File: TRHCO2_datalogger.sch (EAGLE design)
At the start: 31 parts, among them J3 USB-MICROB, U1 ATMEGA328P-MU, U7 SHT31/35, U8 MCP1703/3.3V, Y1 16MHZ

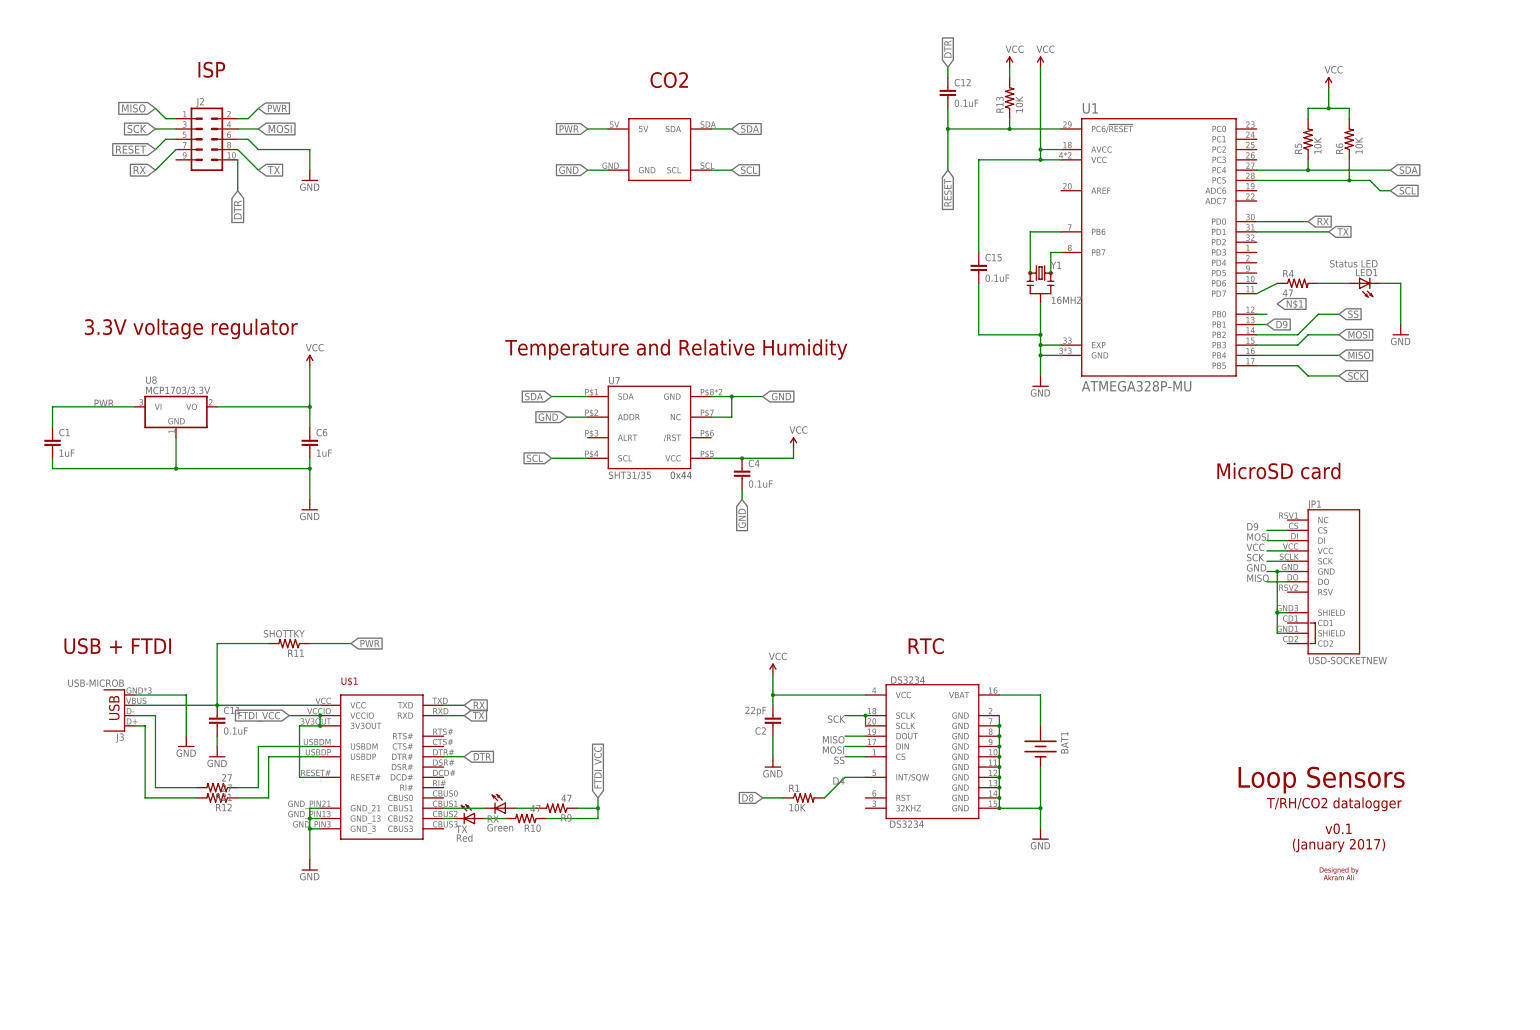
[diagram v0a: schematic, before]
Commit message: Completed v0.1 design
Routed all traces
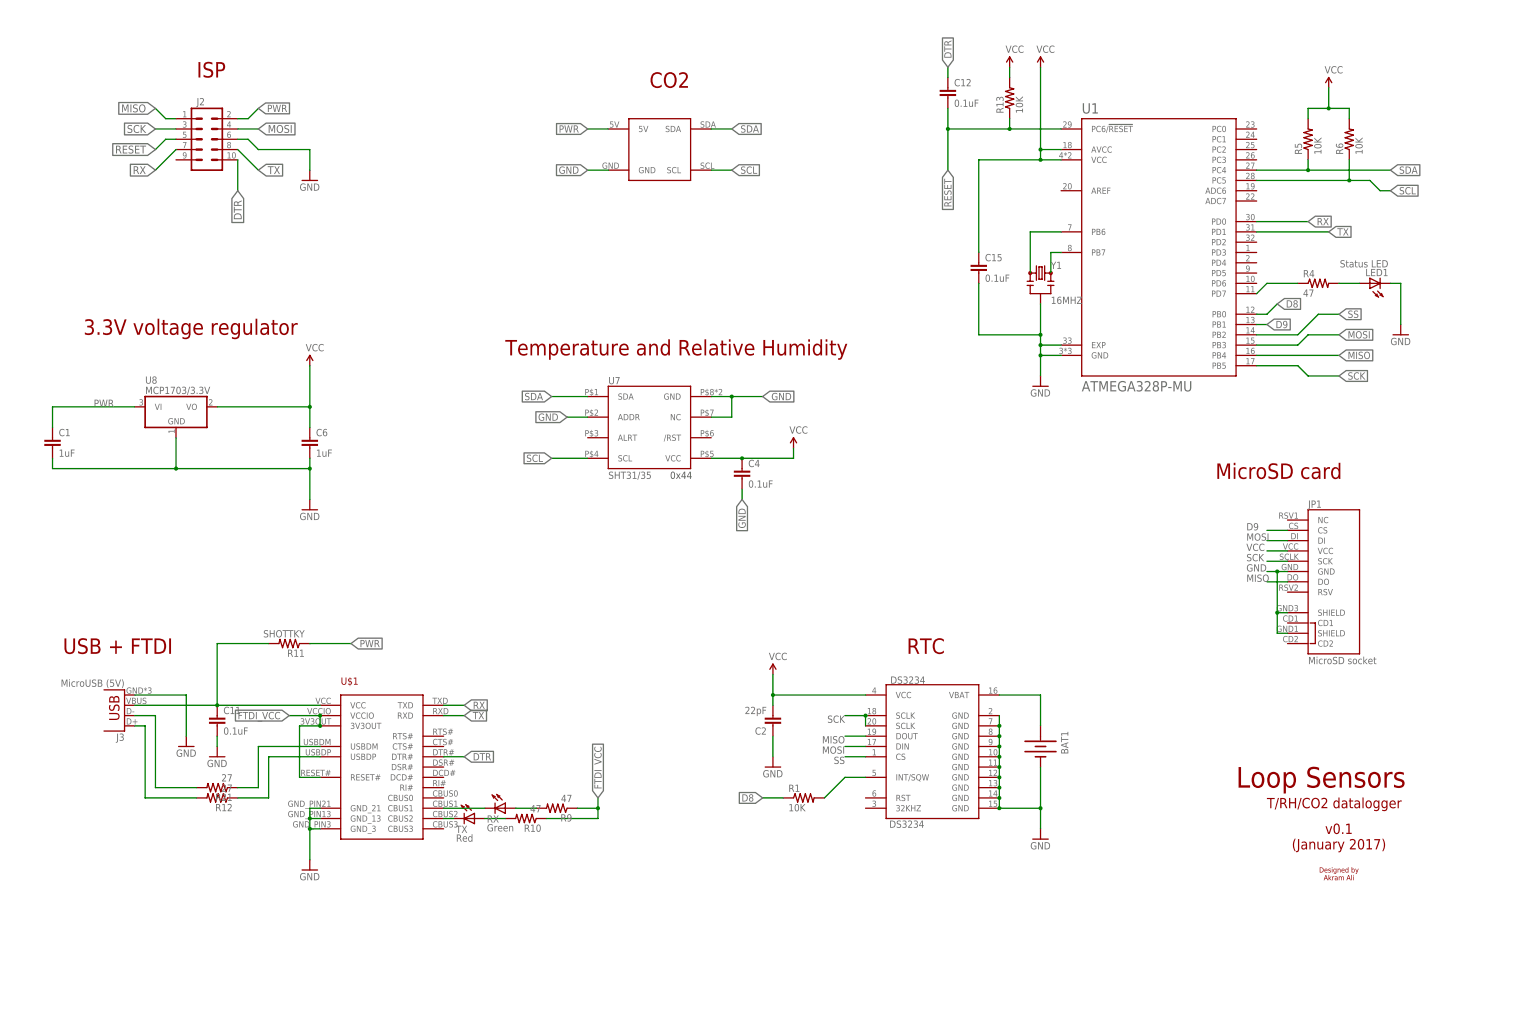
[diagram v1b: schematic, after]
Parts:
- J3: value USB-MICROB -> MicroUSB (5V)
- JP1: value USD-SOCKETNEW -> MicroSD socket
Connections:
- net D4 renamed N$2
- removed net N$1 (its old number): U1.PB0
- net D8: now also U1.PB0
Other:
- moved on the sheet: LED1, R4
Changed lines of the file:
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@@
 </part>
 <part name="GND5" library="SparkFun-Aesthetics" deviceset="GND" device=""/>
-<part name="J3" library="SparkFun-Connectors" deviceset="USB" device="-MICROB">
+<part name="J3" library="SparkFun-Connectors" deviceset="USB" device="-MICROB" value="MicroUSB (5V)">
 <attribute name="MPN" value="CONN-09505"/>
 </part>
@@
 </part>
 <part name="U$3" library="K30-CO2-I2C" deviceset="K30-CO2-I2C" device=""/>
-<part name="JP1" library="SparkFun-Connectors" deviceset="USD-SOCKET" device="NEW"/>
+<part name="JP1" library="SparkFun-Connectors" deviceset="USD-SOCKET" device="NEW" value="MicroSD socket"/>
 <part name="DS3234" library="SparkFun-FreqCtrl" deviceset="DS3234" device=""/>
 <part name="GND3" library="SparkFun-Aesthetics" deviceset="GND" device=""/>
@@
 <instance part="SUPPLY1" gate="G$1" x="182.88" y="119.38"/>
 <instance part="SUPPLY3" gate="G$1" x="121.92" y="25.4"/>
-<instance part="R4" gate="G$1" x="246.38" y="66.04">
-<attribute name="MPN" x="246.38" y="66.04" size="1.778" layer="96" rot="R270" display="off"/>
+<instance part="R4" gate="G$1" x="251.46" y="66.04">
+<attribute name="MPN" x="251.46" y="66.04" size="1.778" layer="96" rot="R270" display="off"/>
 </instance>
 <instance part="R5" gate="G$1" x="248.92" y="101.6" rot="R90">
@@
 </instance>
 <instance part="SUPPLY7" gate="G$1" x="254" y="114.3"/>
-<instance part="LED1" gate="G$1" x="261.62" y="66.04" rot="R90">
-<attribute name="MPN" x="261.62" y="66.04" size="1.778" layer="96" rot="R270" display="off"/>
+<instance part="LED1" gate="G$1" x="264.16" y="66.04" rot="R90">
+<attribute name="MPN" x="264.16" y="66.04" size="1.778" layer="96" rot="R270" display="off"/>
 </instance>
 <instance part="GND8" gate="1" x="271.78" y="53.34"/>
@@
 <pinref part="LED1" gate="G$1" pin="C"/>
 <pinref part="GND8" gate="1" pin="GND"/>
-<wire x1="266.7" y1="66.04" x2="271.78" y2="66.04" width="0.1524" layer="91"/>
+<wire x1="269.24" y1="66.04" x2="271.78" y2="66.04" width="0.1524" layer="91"/>
 <wire x1="271.78" y1="66.04" x2="271.78" y2="55.88" width="0.1524" layer="91"/>
 </segment>
@@
 <pinref part="R4" gate="G$1" pin="2"/>
 <pinref part="LED1" gate="G$1" pin="A"/>
-<wire x1="251.46" y1="66.04" x2="259.08" y2="66.04" width="0.1524" layer="91"/>
+<wire x1="256.54" y1="66.04" x2="261.62" y2="66.04" width="0.1524" layer="91"/>
 </segment>
 </net>
@@
 </segment>
 </net>
-<net name="D4" class="0">
-<segment>
-<pinref part="DS3234" gate="G$1" pin="INT/SQW"/>
-<wire x1="139.7" y1="-55.88" x2="134.62" y2="-55.88" width="0.1524" layer="91"/>
-<label x="134.62" y="-55.88" size="1.778" layer="95" rot="R180"/>
-<pinref part="R1" gate="G$1" pin="2"/>
-<wire x1="134.62" y1="-55.88" x2="129.54" y2="-60.96" width="0.1524" layer="91"/>
-</segment>
-</net>
-<net name="N$9" class="0">
-<segment>
-<pinref part="R4" gate="G$1" pin="1"/>
-<pinref part="U1" gate="G$1" pin="PD7"/>
-<wire x1="236.22" y1="63.5" x2="241.3" y2="66.04" width="0.1524" layer="91"/>
-</segment>
-</net>
 <net name="D9" class="0">
 <segment>
@@
 <net name="D8" class="0">
 <segment>
+<pinref part="U1" gate="G$1" pin="PB0"/>
+<wire x1="236.22" y1="58.42" x2="238.76" y2="58.42" width="0.1524" layer="91"/>
+<label x="241.3" y="60.96" size="1.778" layer="95" xref="yes"/>
+<wire x1="238.76" y1="58.42" x2="241.3" y2="60.96" width="0.1524" layer="91"/>
+</segment>
+<segment>
 <pinref part="R1" gate="G$1" pin="1"/>
 <wire x1="119.38" y1="-60.96" x2="114.3" y2="-60.96" width="0.1524" layer="91"/>
@@
 <net name="N$1" class="0">
 <segment>
-<pinref part="U1" gate="G$1" pin="PB0"/>
-<wire x1="236.22" y1="58.42" x2="238.76" y2="58.42" width="0.1524" layer="91"/>
-<label x="241.3" y="60.96" size="1.778" layer="95" xref="yes"/>
-</segment>
-</net>
+<pinref part="U1" gate="G$1" pin="PD7"/>
+<wire x1="236.22" y1="63.5" x2="238.76" y2="66.04" width="0.1524" layer="91"/>
+<pinref part="R4" gate="G$1" pin="1"/>
+<wire x1="238.76" y1="66.04" x2="246.38" y2="66.04" width="0.1524" layer="91"/>
+</segment>
+</net>
+<net name="N$2" class="0">
+<segment>
+<pinref part="DS3234" gate="G$1" pin="INT/SQW"/>
+<pinref part="R1" gate="G$1" pin="2"/>
+<wire x1="139.7" y1="-55.88" x2="134.62" y2="-55.88" width="0.1524" layer="91"/>
+<wire x1="134.62" y1="-55.88" x2="129.54" y2="-60.96" width="0.1524" layer="91"/>
+</segment>
+</net>

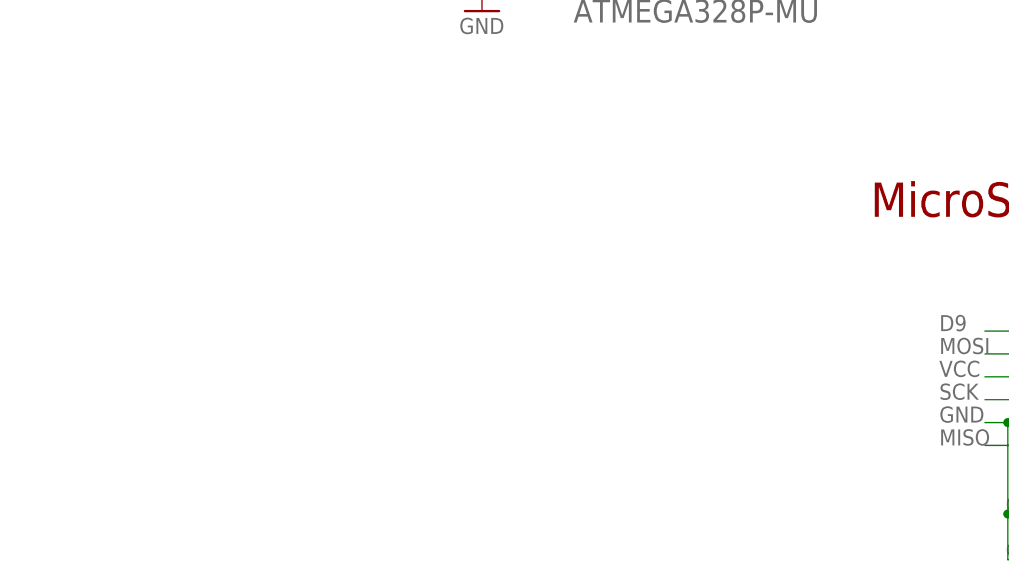
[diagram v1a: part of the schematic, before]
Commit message: Added D battery input headers
Requires boost converter (https://www.sparkfun.com/products/10255) to allow 2 D batteries to supply at least 3V and get output 5V, 500mA
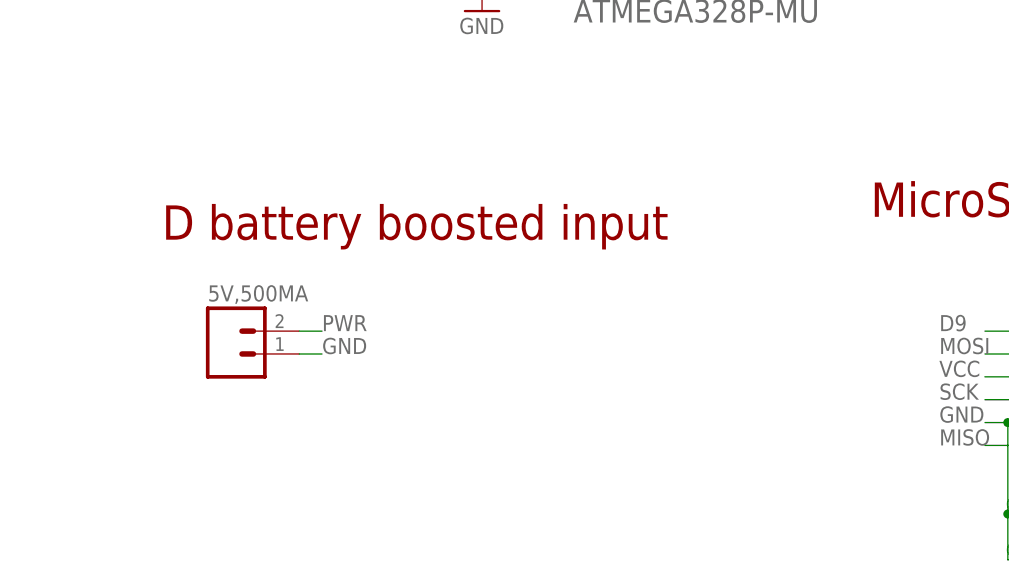
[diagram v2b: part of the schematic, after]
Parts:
- added 5V,500MA: (no value), SparkFun-Connectors:M02PTH
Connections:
- net GND: now also 5V,500MA.1
- net PWR: now also 5V,500MA.2
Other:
- note added: "D battery boosted input"
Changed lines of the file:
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@@
 <attribute name="MPN" value="RC0805JR-0747RL"/>
 </part>
+<part name="5V,500MA" library="SparkFun-Connectors" deviceset="M02" device="PTH"/>
 </parts>
 <sheets>
@@
 <text x="226.06" y="17.78" size="3.81" layer="94">MicroSD card</text>
 <text x="149.86" y="-25.4" size="3.81" layer="94">RTC</text>
+<text x="147.32" y="15.24" size="3.81" layer="94">D battery boosted input</text>
 </plain>
 <instances>
@@
 <attribute name="MPN" x="124.46" y="-60.96" size="1.778" layer="96" rot="R270" display="off"/>
 </instance>
+<instance part="5V,500MA" gate="G$1" x="154.94" y="2.54"/>
 </instances>
 <busses>
@@
 <junction x="241.3" y="-15.24"/>
 </segment>
+<segment>
+<pinref part="5V,500MA" gate="G$1" pin="1"/>
+<wire x1="162.56" y1="2.54" x2="165.1" y2="2.54" width="0.1524" layer="91"/>
+<label x="165.1" y="2.54" size="1.778" layer="95"/>
+</segment>
 </net>
 <net name="VCC" class="0">
@@
 <label x="71.12" y="104.14" size="1.778" layer="95" rot="R180" xref="yes"/>
 </segment>
-</net>
+<segment>
+<pinref part="5V,500MA" gate="G$1" pin="2"/>
+<wire x1="162.56" y1="5.08" x2="165.1" y2="5.08" width="0.1524" layer="91"/>
+<label x="165.1" y="5.08" size="1.778" layer="95"/>
+</segment>
+</net>

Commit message: Traces adjusted
Cleared some spacing between traces and vias
Added MPN for some components
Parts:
- BAT1: MPN (none) -> 3000
- DS3234: MPN (none) -> DS3234S#
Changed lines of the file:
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@@
 <part name="U$3" library="K30-CO2-I2C" deviceset="K30-CO2-I2C" device=""/>
 <part name="JP1" library="SparkFun-Connectors" deviceset="USD-SOCKET" device="NEW" value="MicroSD socket"/>
-<part name="DS3234" library="SparkFun-FreqCtrl" deviceset="DS3234" device=""/>
+<part name="DS3234" library="SparkFun-FreqCtrl" deviceset="DS3234" device="">
+<attribute name="MPN" value="DS3234S#"/>
+</part>
 <part name="GND3" library="SparkFun-Aesthetics" deviceset="GND" device=""/>
 <part name="SUPPLY2" library="SparkFun-Aesthetics" deviceset="VCC" device=""/>
 <part name="U1" library="ATMEGA328P-MU" deviceset="ATMEGA328P-MU" device=""/>
-<part name="BAT1" library="SparkFun-Electromechanical" deviceset="BATTERY" device="12MM"/>
+<part name="BAT1" library="SparkFun-Electromechanical" deviceset="BATTERY" device="12MM">
+<attribute name="MPN" value="3000"/>
+</part>
 <part name="C2" library="SparkFun-Passives" deviceset="CAP" device="0805" value="22pF">
 <attribute name="MPN" value="AC0805KRX7R9BB104"/>
@@
 <instance part="U$3" gate="G$1" x="88.9" y="99.06"/>
 <instance part="JP1" gate="G$1" x="251.46" y="-5.08"/>
-<instance part="DS3234" gate="G$1" x="154.94" y="-48.26"/>
+<instance part="DS3234" gate="G$1" x="154.94" y="-48.26">
+<attribute name="MPN" x="154.94" y="-48.26" size="1.778" layer="96" display="off"/>
+</instance>
 <instance part="GND3" gate="1" x="182.88" y="-71.12"/>
 <instance part="SUPPLY2" gate="G$1" x="116.84" y="-30.48"/>
 <instance part="U1" gate="G$1" x="213.36" y="76.2"/>
-<instance part="BAT1" gate="G$1" x="182.88" y="-48.26" rot="R270"/>
+<instance part="BAT1" gate="G$1" x="182.88" y="-48.26" rot="R270">
+<attribute name="MPN" x="182.88" y="-48.26" size="1.778" layer="96" rot="R270" display="off"/>
+</instance>
 <instance part="C2" gate="G$1" x="116.84" y="-40.64" rot="R180">
 <attribute name="MPN" x="116.84" y="-40.64" size="1.778" layer="96" rot="R90" display="off"/>
